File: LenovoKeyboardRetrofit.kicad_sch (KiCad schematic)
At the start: 3 parts

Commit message: Modification of sch
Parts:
- removed U?: RP2040, 03_ICs:QFN-56-1EP_7x7mm_P0.4mm_EP5.6x5.6mm, symbol 06_ICs:RP2040
- added U?: RP2040, 03_ICs:QFN-56-1EP_7x7mm_P0.4mm_EP5.6x5.6mm, symbol 06_ICs:RP2040
- FLASH?: symbol 09_Memory:W25Q16JVSSIQ -> 09_Memory:FLASH_W25Q16JVSSIQ
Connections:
- net QSPI_IO1: now reaches FLASH?.2 (DO(IO1))
- net QSPI_IO1: now also U?.55 (QSPI_SD1)
- net QSPI_IO2: now reaches FLASH?.3 (NWP(IO2))
- net QSPI_IO2: now also U?.54 (QSPI_SD2)
- net VSS: now reaches FLASH?.4 (GND)
- net VSS: now also U?.57 (GND)
- net QSPI_IO0: now reaches FLASH?.5 (DI(IO0))
- net QSPI_IO0: now also U?.53 (QSPI_SD0)
- net QSPI_IO3: now reaches FLASH?.7 (NRST(IO3))
- net QSPI_IO3: now also U?.51 (QSPI_SD3)
- net +3.3V: now reaches FLASH?.8 (VCC)
- new net QSPI_CLK: U?.52 (QSPI_SCLK)
- new net QSPI_SS: U?.56 (QSPI_SS)
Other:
- moved on the sheet: FLASH?

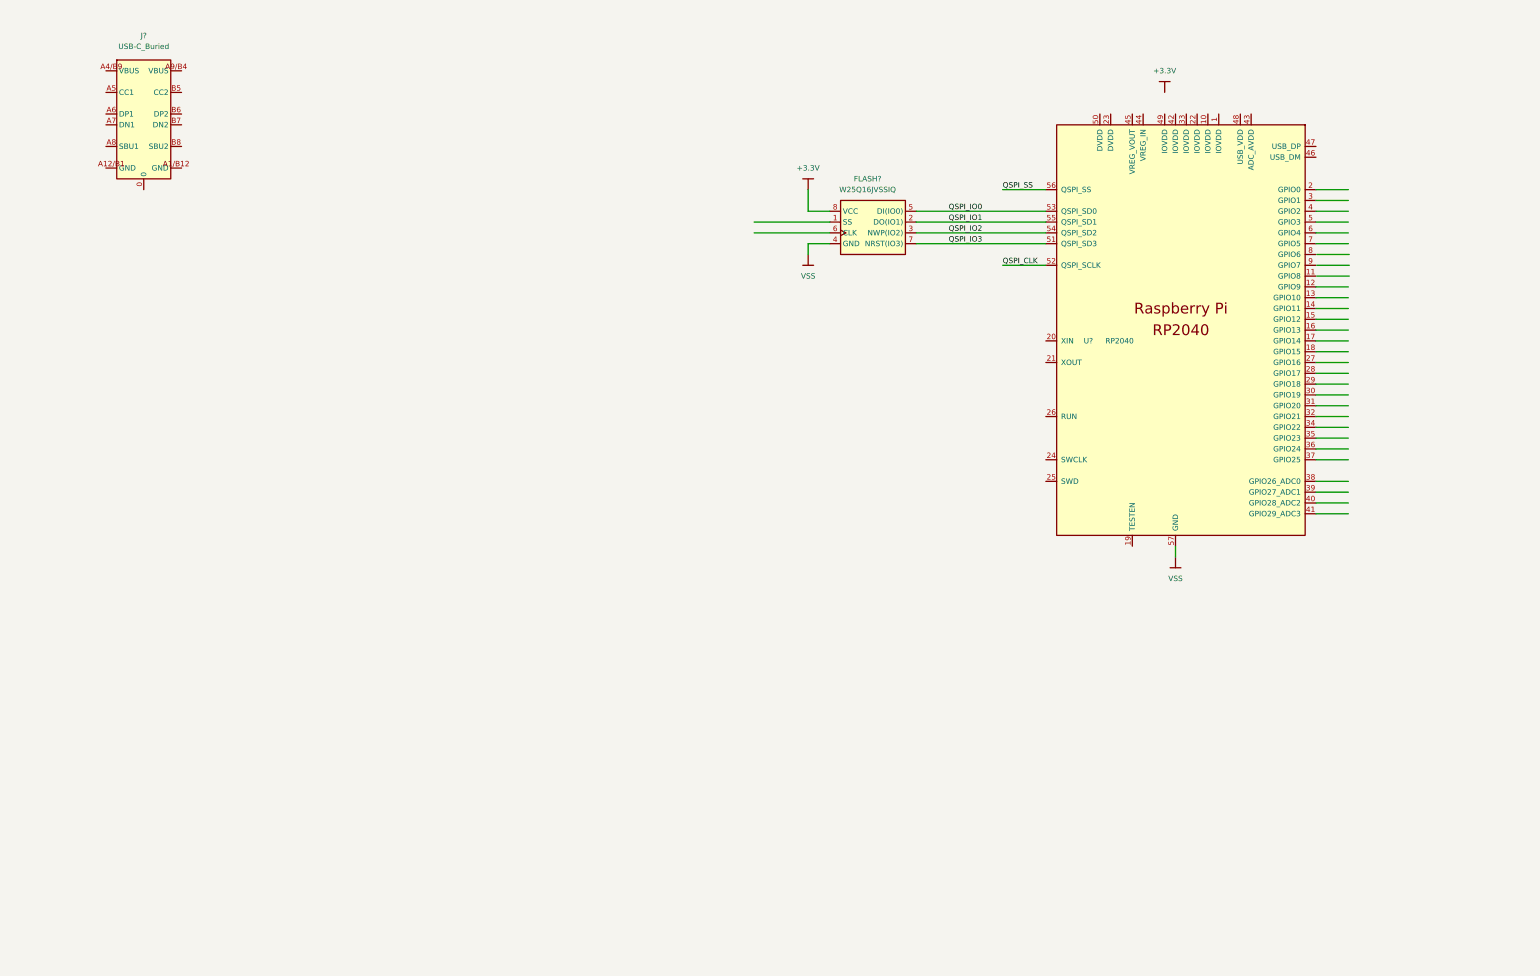
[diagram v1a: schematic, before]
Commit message: Adding of TUSB usb hub
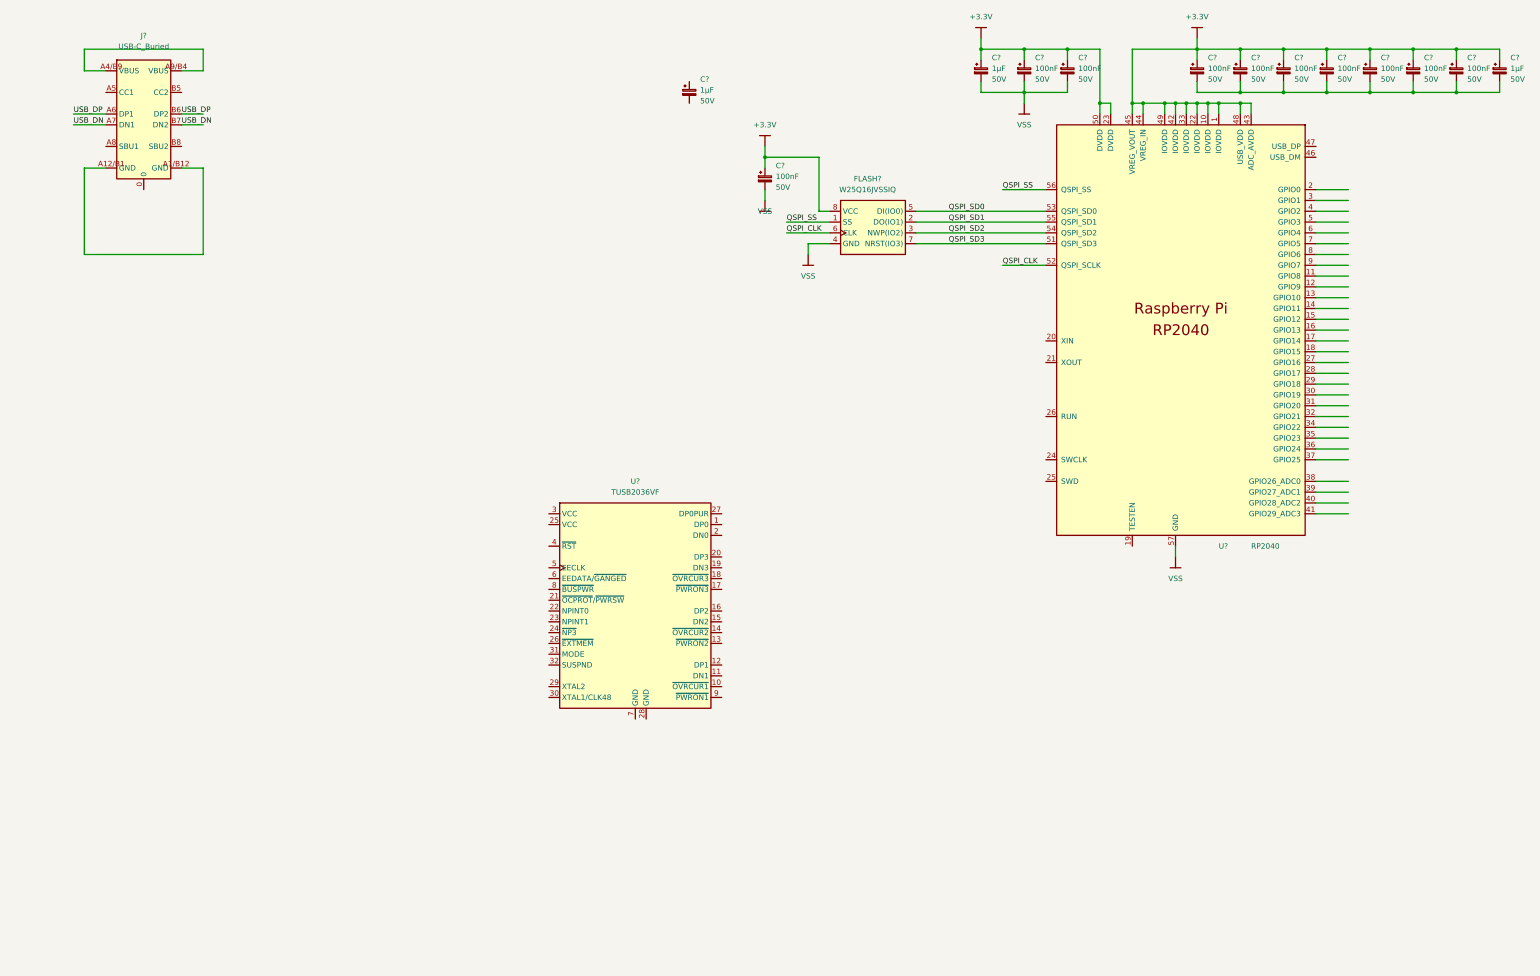
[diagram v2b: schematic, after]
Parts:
- added C? (x3): CAP_0603_1uF_50V, 01_Passives:CAP_0603, symbol 01_Capacitor:CAP_0603_1uF_50V
- added C? (x10): CAP_0603_100nF_50V, 01_Passives:CAP_0603, symbol 01_Capacitor:CAP_0603_100nF_50V
- added U?: TUSB2036VF, 03_ICs:LQFP-32_7x7mm_P0.8mm, symbol 06_ICs:TUSB2036VF
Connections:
- net +3.3V: now also U?.1 (IOVDD), U?.10 (IOVDD), U?.22 (IOVDD), U?.23 (DVDD), U?.33 (IOVDD), U?.42 (IOVDD), U?.43 (ADC_AVDD), U?.44 (VREG_IN), U?.45 (VREG_VOUT), U?.48 (USB_VDD), U?.49 (IOVDD), U?.50 (DVDD), C?.1, C?.1, C?.1, C?.1, C?.1, C?.1, C?.1, C?.1, C?.1, C?.1, C?.1, C?.1
- net QSPI_CLK: now also FLASH?.6 (CLK)
- net QSPI_SS: now also FLASH?.1 (SS)
- net VSS: now also C?.2, C?.2, C?.2, C?.2
- net at J?.A1/B12 (GND): now also J?.A12/B1 (GND)
- net at J?.A4/B9 (VBUS): now also J?.A9/B4 (VBUS)
- net USB_DP: now reaches J?.A6 (DP1)
- net USB_DP: now also J?.B6 (DP2)
- net USB_DN: now reaches J?.A7 (DN1)
- net USB_DN: now also J?.B7 (DN2)
- net QSPI_IO0 renamed QSPI_SD0
- net QSPI_IO1 renamed QSPI_SD1
- net QSPI_IO2 renamed QSPI_SD2
- net QSPI_IO3 renamed QSPI_SD3
- new net: C?.2, C?.2, C?.2, C?.2, C?.2, C?.2, C?.2, C?.2

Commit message: First config of TUSB
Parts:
- added C1, C3, C4: CAP_0603_100nF_50V, 01_Passives:CAP_0603, symbol 01_Capacitor:CAP_0603_100nF_50V
- added C2: CAP_0603_1uF_50V, 01_Passives:CAP_0603, symbol 01_Capacitor:CAP_0603_1uF_50V
- added R1, R2, R3: RES_0603_27R_1%, 01_Passives:RES_0603, symbol 02_Resistor:RES_0603_27R_1%
- added R10, R12, R4, R5, R6, R7, R8, R9: RES_0603_10K_1%, 01_Passives:RES_0603, symbol 02_Resistor:RES_0603_10K_1%
- added R11: (no value), symbol 02_Resistor:RES_0603_10K_1%
- added R13, R14: (no value), symbol 02_Resistor:RES_0603_27R_1%
- added X1: (no value), symbol 08_Crystal:X_12MHz_20pF_10ppm
- gave numbers to parts that had none: 17
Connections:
- net +3.3V: now also U1.25 (VCC), U1.3 (VCC), C2.1, C3.1, C4.1, R11.1, R4.1, R7.1, R8.1
- net VSS: now also J1.A1/B12 (GND), J1.A12/B1 (GND), U1.28 (GND), U1.7 (GND), U2.19 (TESTEN), C1.2, C2.2, C3.2, C4.2, R1.1, R10.1, R12.1, R5.1, R6.1, R9.1, X1.2 (GND), X1.4 (GND)
- net USB1_OVRCUR: now reaches U1.10 (~{OVRCUR1})
- net USB1_DN: now reaches U1.11 (DN1)
- net USB1_DP: now reaches U1.12 (DP1)
- net USB2_PWR: now reaches U1.13 (~{PWRON2})
- net USB2_OVRCUR: now reaches U1.14 (~{OVRCUR2})
- net USB2_DN: now reaches U1.15 (DN2)
- net USB2_DP: now reaches U1.16 (DP2)
- net USB3_PWR: now reaches U1.17 (~{PWRON3})
- net USB3_OVRCUR: now reaches U1.18 (~{OVRCUR3})
- net USB3_DN: now reaches U1.19 (DN3)
- net USB3_DP: now reaches U1.20 (DP3)
- net at U1.21 (~{OCPROT}/~{PWRSW}): now also R7.2
- net at U1.22 (NPINT0): now also R8.2
- net at U1.23 (NPINT1): now also R9.2
- net at U1.24 (~{NP3}): now also R10.2
- net at U1.26 (~{EXTMEM}): now also R11.2
- net at U1.31 (MODE): now also R12.2
- net TUSB_~{RST}: now reaches U1.4 (~{RST})
- net TUSB_~{RST}: now also C1.1, R4.2
- net at U1.6 (EEDATA/~{GANGED}): now also R5.2
- net at U1.8 (~{BUSPWR}): now also R6.2
- net USB1_PWR: now reaches U1.9 (~{PWRON1})
- net at J1.0: now also R1.2
- net at U2.20 (XIN): now also X1.1 (X1)
- net at U2.21 (XOUT): now also X1.3 (X2)
- net at U2.46 (USB_DM): now also R14.1
- net at U2.47 (USB_DP): now also R13.1
- net USB_DN renamed US_USB_DN
- net US_USB_DN: now also R3.1
- net USB_DP renamed US_USB_DP
- net US_USB_DP: now also R2.1
- new net RPI_USB_DN: R14.2
- new net RPI_USB_DP: R13.2
- new net USB0_DN: R3.2
- new net USB0_DP: R2.2
- no-connect marks 0 -> 1
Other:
- moved on the sheet: U1

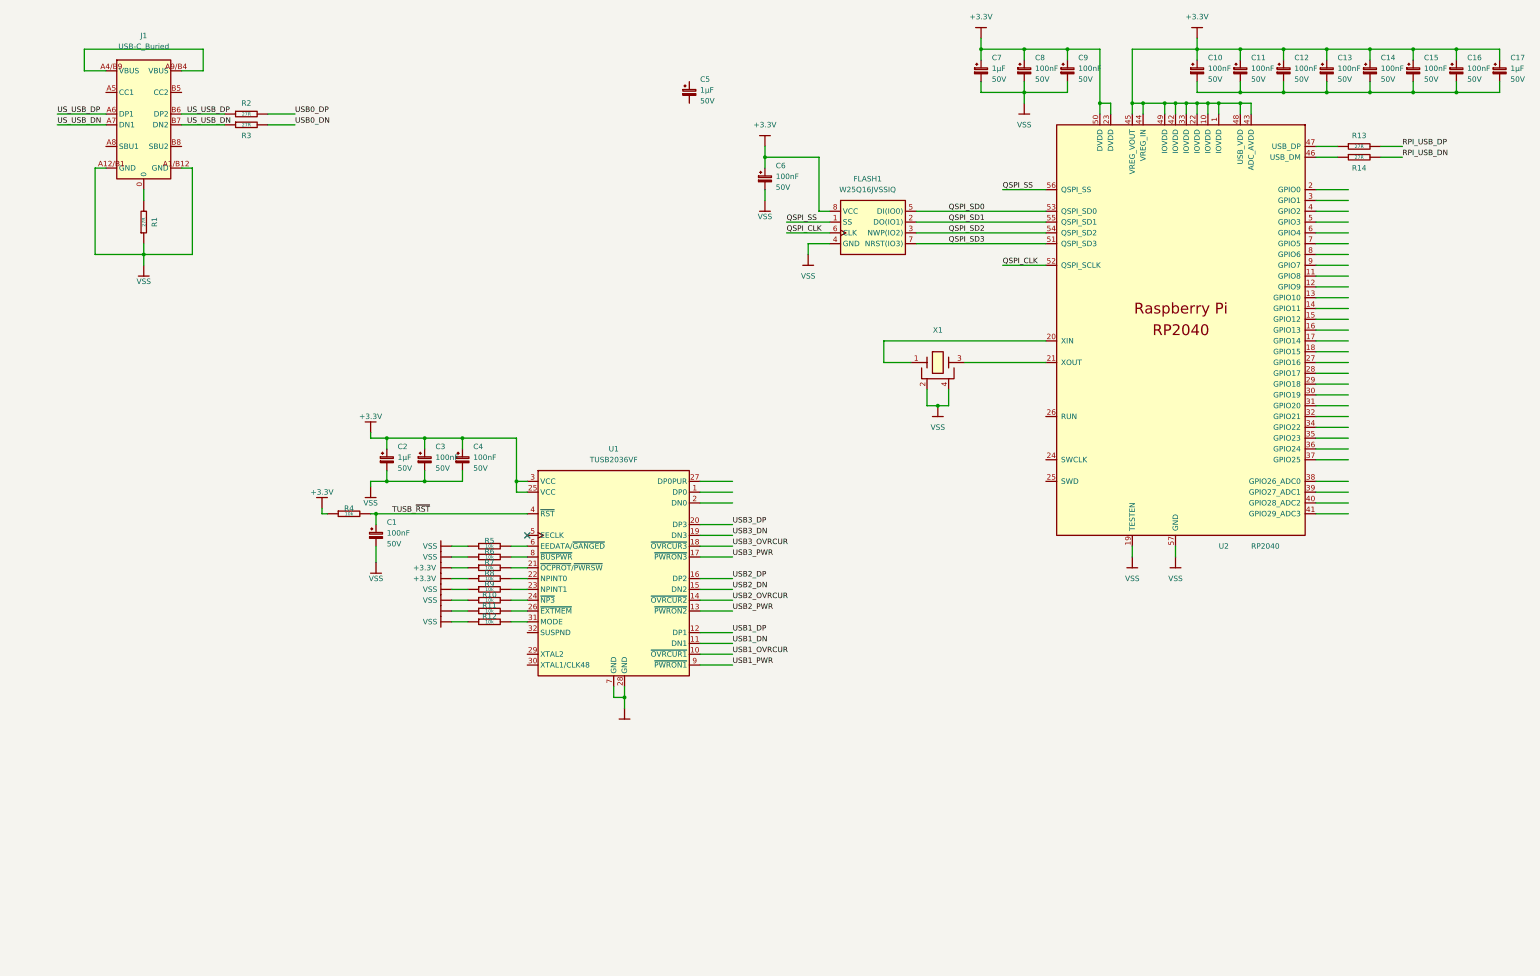
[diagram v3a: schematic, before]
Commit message: USB connectors
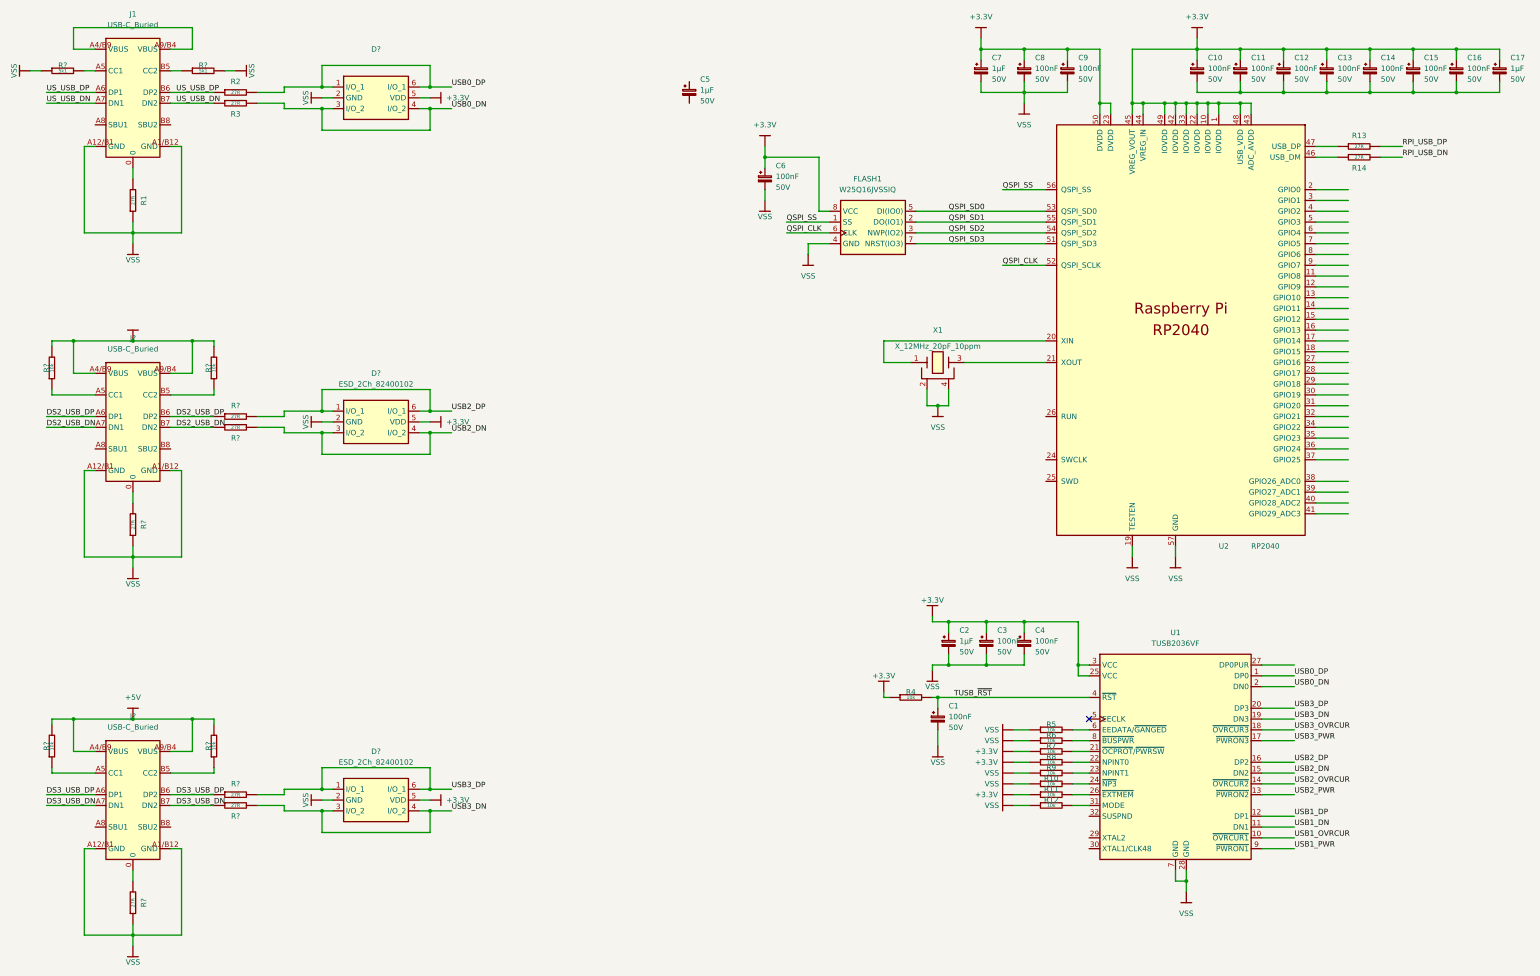
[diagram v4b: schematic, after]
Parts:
- added D?: (no value), symbol 04_Diodes:ESD_2Ch_82400102
- added D? (x2): ESD_2Ch_82400102, 03_ICs:SOT-23-6, symbol 04_Diodes:ESD_2Ch_82400102
- added J? (x2): USB-C_Buried, 02_Connectors:USB4510, symbol 07_Connectors:USB-C_Buried
- added R?: RES_0603_5K1_1%, 01_Passives:RES_0603, symbol 02_Resistor:RES_0603_5K1_1%
- added R? (x6): RES_0603_27R_1%, 01_Passives:RES_0603, symbol 02_Resistor:RES_0603_27R_1%
- added R? (x3): RES_0603_10K_1%, 01_Passives:RES_0603, symbol 02_Resistor:RES_0603_10K_1%
- added R?: (no value), symbol 02_Resistor:RES_0603_10K_1%
- added R?: (no value), symbol 02_Resistor:RES_0603_5K1_1%
- R11: value (none) -> RES_0603_10K_1%; footprint (none) -> 01_Passives:RES_0603
- R13, R14: value (none) -> RES_0603_27R_1%; footprint (none) -> 01_Passives:RES_0603
- X1: value (none) -> X_12MHz_20pF_10ppm
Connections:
- net +3.3V: now also D?.5 (VDD), D?.5 (VDD), D?.5 (VDD)
- net USB0_DN: now also U1.2 (DN0), D?.3 (I/O_2), D?.4 (I/O_2)
- net USB0_DP: now also U1.1 (DP0), D?.1 (I/O_1), D?.6 (I/O_1)
- net USB2_DN: now also D?.3 (I/O_2), D?.4 (I/O_2), R?.2
- net USB2_DP: now also D?.1 (I/O_1), D?.6 (I/O_1), R?.2
- net USB3_DN: now also D?.3 (I/O_2), D?.4 (I/O_2), R?.2
- net USB3_DP: now also D?.1 (I/O_1), D?.6 (I/O_1), R?.2
- net VSS: now also D?.2 (GND), D?.2 (GND), D?.2 (GND), J?.A1/B12 (GND), J?.A1/B12 (GND), J?.A12/B1 (GND), J?.A12/B1 (GND), R?.1, R?.1, R?.1, R?.2
- net at J1.A5 (CC1): now also R?.2
- net at J1.B5 (CC2): now also R?.1
- new net: J?.B5 (CC2), R?.1 (x2)
- new net: J?.0, R?.2 (x2)
- new net: J?.A5 (CC1), R?.1 (x2)
- new net +5V: J?.A4/B9 (VBUS), J?.A4/B9 (VBUS), J?.A9/B4 (VBUS), J?.A9/B4 (VBUS), R?.2, R?.2, R?.2, R?.2
- new net DS2_USB_DN: J?.A7 (DN1), J?.B7 (DN2), R?.1
- new net DS2_USB_DP: J?.A6 (DP1), J?.B6 (DP2), R?.1
- new net DS3_USB_DN: J?.A7 (DN1), J?.B7 (DN2), R?.1
- new net DS3_USB_DP: J?.A6 (DP1), J?.B6 (DP2), R?.1
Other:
- moved on the sheet: C1, C2, C3, C4, J1, R1, R10, R11, R12, R2, R3, R4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
